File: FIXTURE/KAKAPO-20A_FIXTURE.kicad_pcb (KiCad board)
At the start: 2 copper layers, 100 x 100 mm, 59 parts, among them J1 Conn_01x03, J10 Pins_2.54_1x2, J2 Conn_01x03, J3 Conn_01x03, J4 Conn_01x03, J5 Pins_2.54_1x2, J7 Conn_01x03, J8 Conn_01x03, M1 Mount_M3, M10 Mount_M3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

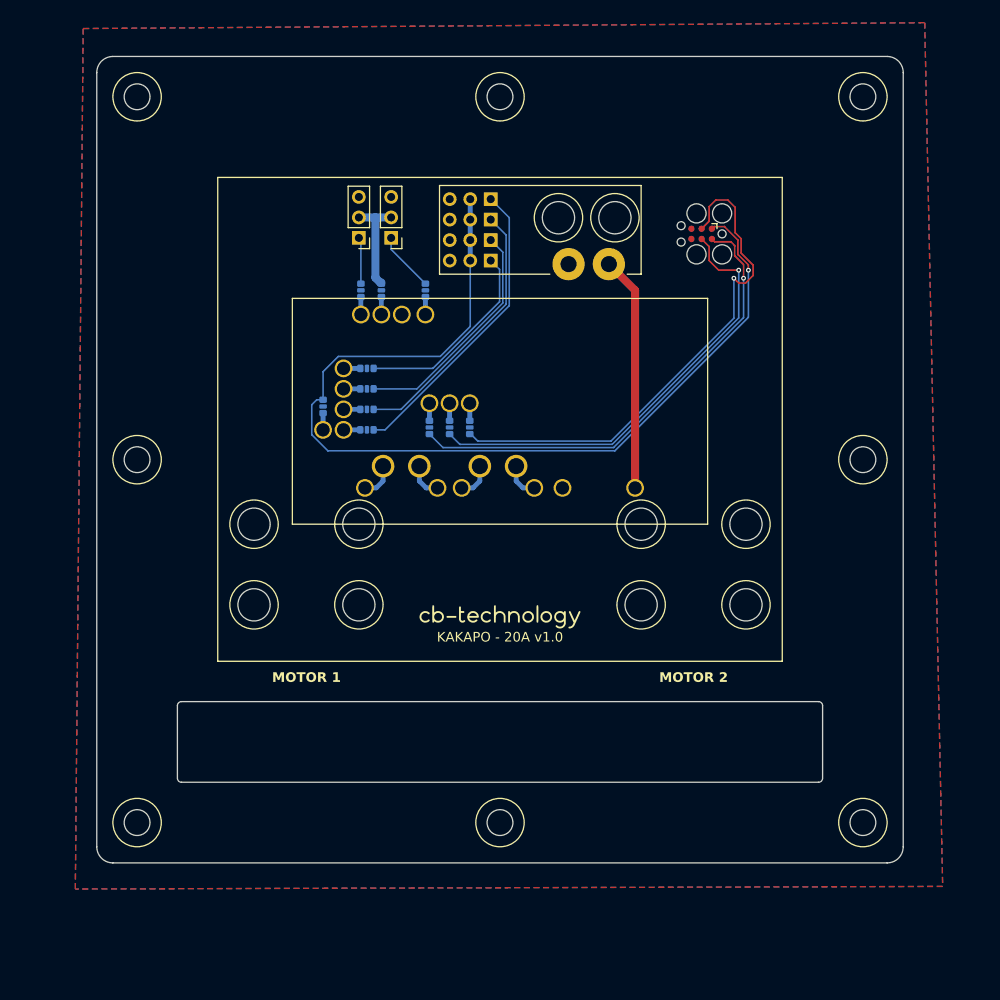
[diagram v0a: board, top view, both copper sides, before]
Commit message: Update Fixture Design to Be Inline With Other Jigs
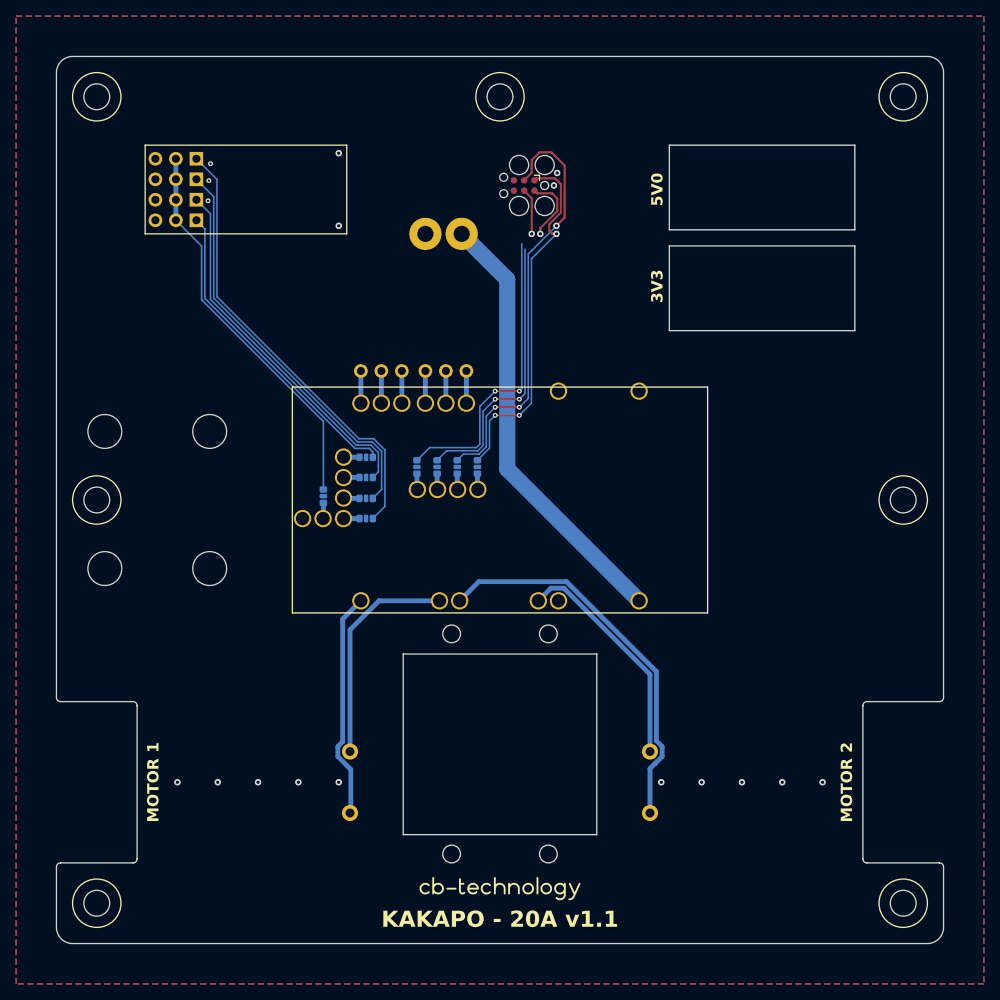
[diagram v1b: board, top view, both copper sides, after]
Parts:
- removed R11, R12, R13, R18, R8: 0R, R_Resistor:R_0603
- added M19: Mount_M3, M_Mechanical:Mount_M3, F.Cu at (184.0, 136.5)
- added M20: Mount_M3, M_Mechanical:Mount_M3, F.Cu at (171.0, 153.5)
- added M21: Mount_M3, M_Mechanical:Mount_M3, F.Cu at (184.0, 153.5)
- added M22: Mount_M3, M_Mechanical:Mount_M3, F.Cu at (214.0, 161.6)
- added M23: Mount_M3, M_Mechanical:Mount_M3, F.Cu at (226.0, 161.6)
- added M24: Mount_M3, M_Mechanical:Mount_M3, F.Cu at (214.0, 188.9)
- added M25: Mount_M3, M_Mechanical:Mount_M3, F.Cu at (226.0, 188.9)
- added R1: 0R, R_Resistor:R_0603, B.Cu at (203.4, 147.3)
- added R2: 0R, R_Resistor:R_0603, B.Cu at (203.4, 144.8)
- added R3: 0R, R_Resistor:R_0603, B.Cu at (198.1, 144.5)
- added TP10: TestPoint, TestPoint:TestPoint_THTPad_D3.0mm_Drill1.5mm, F.Cu at (198.1, 147.3)
- added TP12: TestPoint, TestPoint:TestPoint_THTPad_D3.0mm_Drill1.5mm, F.Cu at (195.5, 147.3)
- added TP20: TestPoint, TestPoint:TestPoint_THTPad_D3.0mm_Drill1.5mm, F.Cu at (227.2, 131.5)
- added TP21: TestPoint, TestPoint:TestPoint_THTPad_D3.0mm_Drill1.5mm, F.Cu at (237.2, 131.5)
- added TP8: TestPoint, TestPoint:TestPoint_THTPad_D3.0mm_Drill1.5mm, F.Cu at (200.6, 147.3)
- added TP9: TestPoint, TestPoint:TestPoint_THTPad_D3.0mm_Drill1.5mm, F.Cu at (200.6, 144.8)
- J1, J4: moved to B.Cu
- moved M8 103.0 mm to (170.0, 95.0)
- moved J5 42.9 mm to (238.5, 180.0), turned to 0 degrees
- moved M5 41.7 mm to (171.0, 136.5)
- moved J10 39.9 mm to (201.4, 180.0), turned to 0 degrees
- moved M17 39.1 mm to (253.5, 187.0), turned to 90 degrees
- moved J2 36.8 mm to (182.3, 102.7)
- moved J3 36.8 mm to (182.3, 105.2)
- moved J7 36.8 mm to (182.3, 107.8)
- moved J8 36.8 mm to (182.3, 110.3)
- moved G*** 33.7 mm to (220.0, 193.2)
- moved TP30 33.2 mm to (215.5, 112.0), turned to 0 degrees
- moved M14 30.0 mm to (195.0, 187.0), turned to 90 degrees
- moved M16 30.0 mm to (245.0, 187.0), turned to 90 degrees
- moved M10 29.2 mm to (186.5, 187.0), turned to 90 degrees
- moved M13 26.1 mm to (195.0, 173.0), turned to 90 degrees
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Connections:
- J1 pad 2: /5V0 -> /5V0_S1
- J2 pad 2: /3V3 -> /5V0
- J3 pad 2: /3V3 -> /5V0
- J4 pad 2: /5V0 -> /5V0_S2
- J7 pad 2: /3V3 -> /5V0
- J8 pad 2: /3V3 -> /5V0
- TP1 pad 1: Net-(R11-Pad1) -> /GND
- TP15 pad 1: Net-(R8-Pad1) -> /5V0_S1
- TP2 pad 1: Net-(R12-Pad1) -> /5V0_S2
- TP3 pad 1: Net-(R13-Pad1) -> /OUT1
- TP4 pad 1: Net-(R18-Pad1) -> /OUT2
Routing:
- net /3V3: track 121.1 -> 45.0 mm, vias 1 -> 3
- net /MOTOR_2+: track 4.45 -> 48.5 mm
- net /5V0: track 12.5 -> 48.6 mm
- net /BATT+: track 29.3 -> 54.6 mm
- net /MOTOR_2-: track 4.45 -> 28.5 mm
- net /MOTOR_1+: track 4.45 -> 28.2 mm
- net /MOTOR_1-: track 4.45 -> 27.7 mm
- net /SIGNAL1: track 37.4 -> 56.0 mm
- net /SIGNAL2: track 33.1 -> 50.6 mm
- net /SIGNAL3: track 28.9 -> 45.1 mm
- net /SWDCLK: track 56.0 -> 40.5 mm, vias 1 -> 3
- net /SIGNAL4: track 24.6 -> 39.5 mm
- net /SWDIO: track 58.9 -> 46.0 mm, vias 1 -> 3
- net /nRST: track 63.9 -> 53.0 mm, vias 1 -> 3
- net /GND: track 0.00 -> 8.00 mm, vias 0 -> 17
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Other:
- board size 100 x 100 mm -> 110 x 110 mm
- board text added: "3V3"
- board text added: "5V0"
- board text added: "KAKAPO - 20A v1.1"
- board text removed: "KAKAPO - 20A v1.0"
